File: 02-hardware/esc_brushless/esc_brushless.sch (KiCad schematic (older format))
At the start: 17 parts

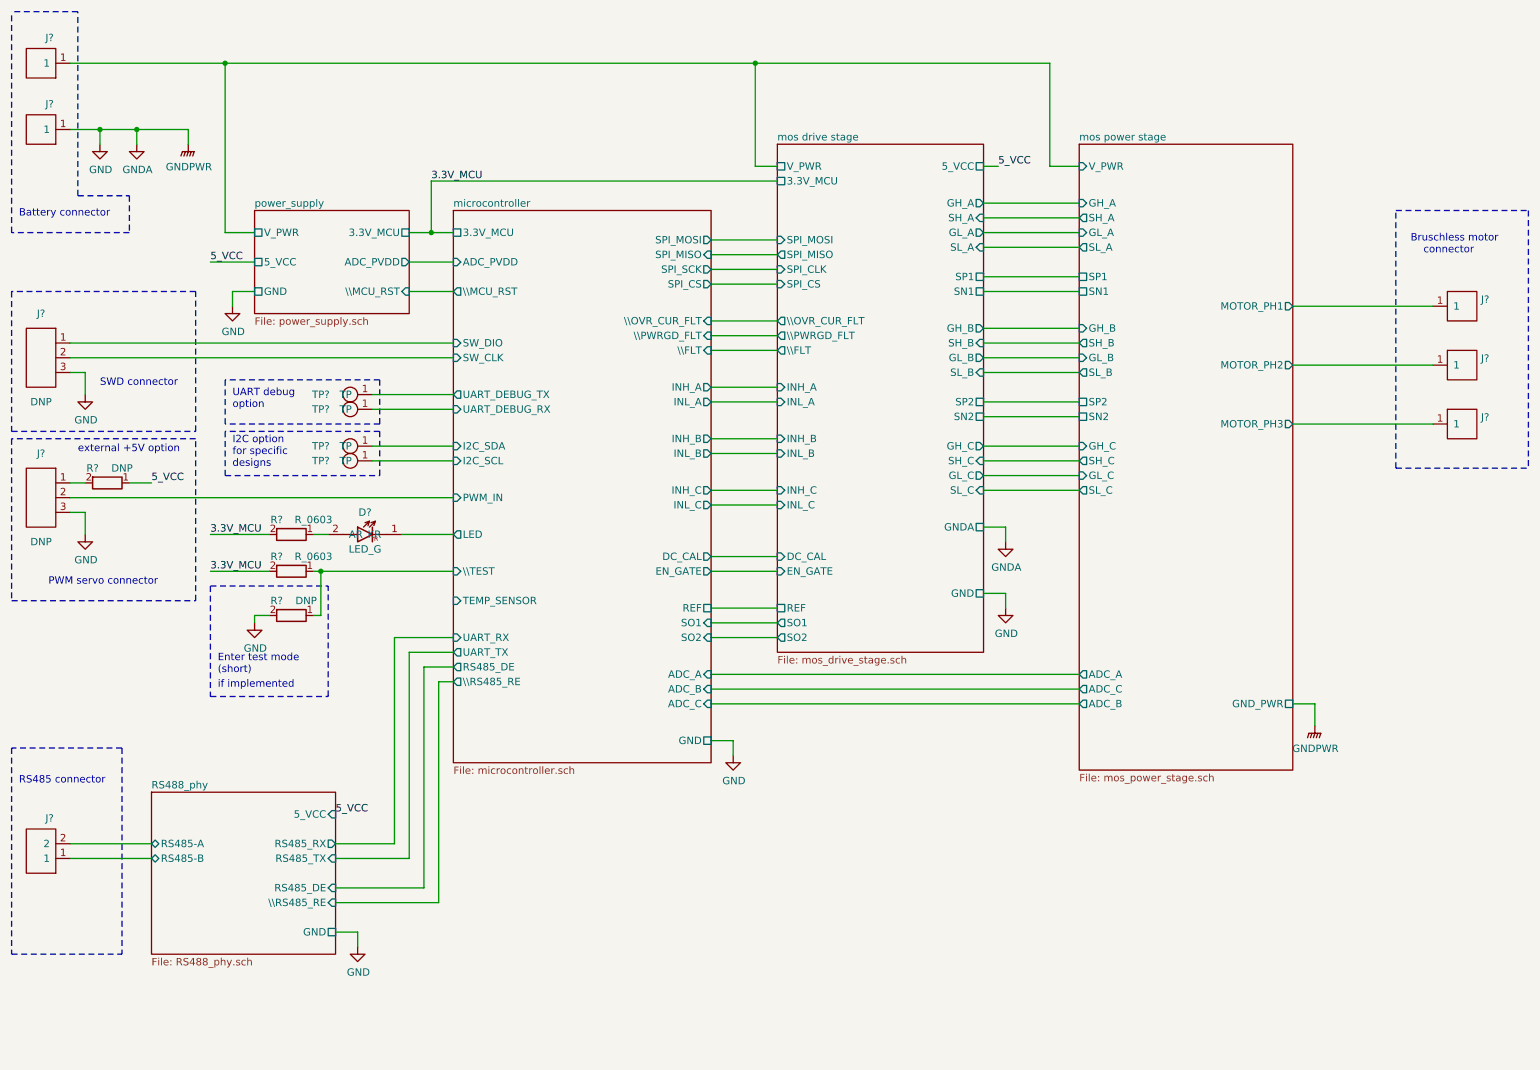
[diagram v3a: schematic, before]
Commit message: Schematics v1.0 - Fix DRC issues
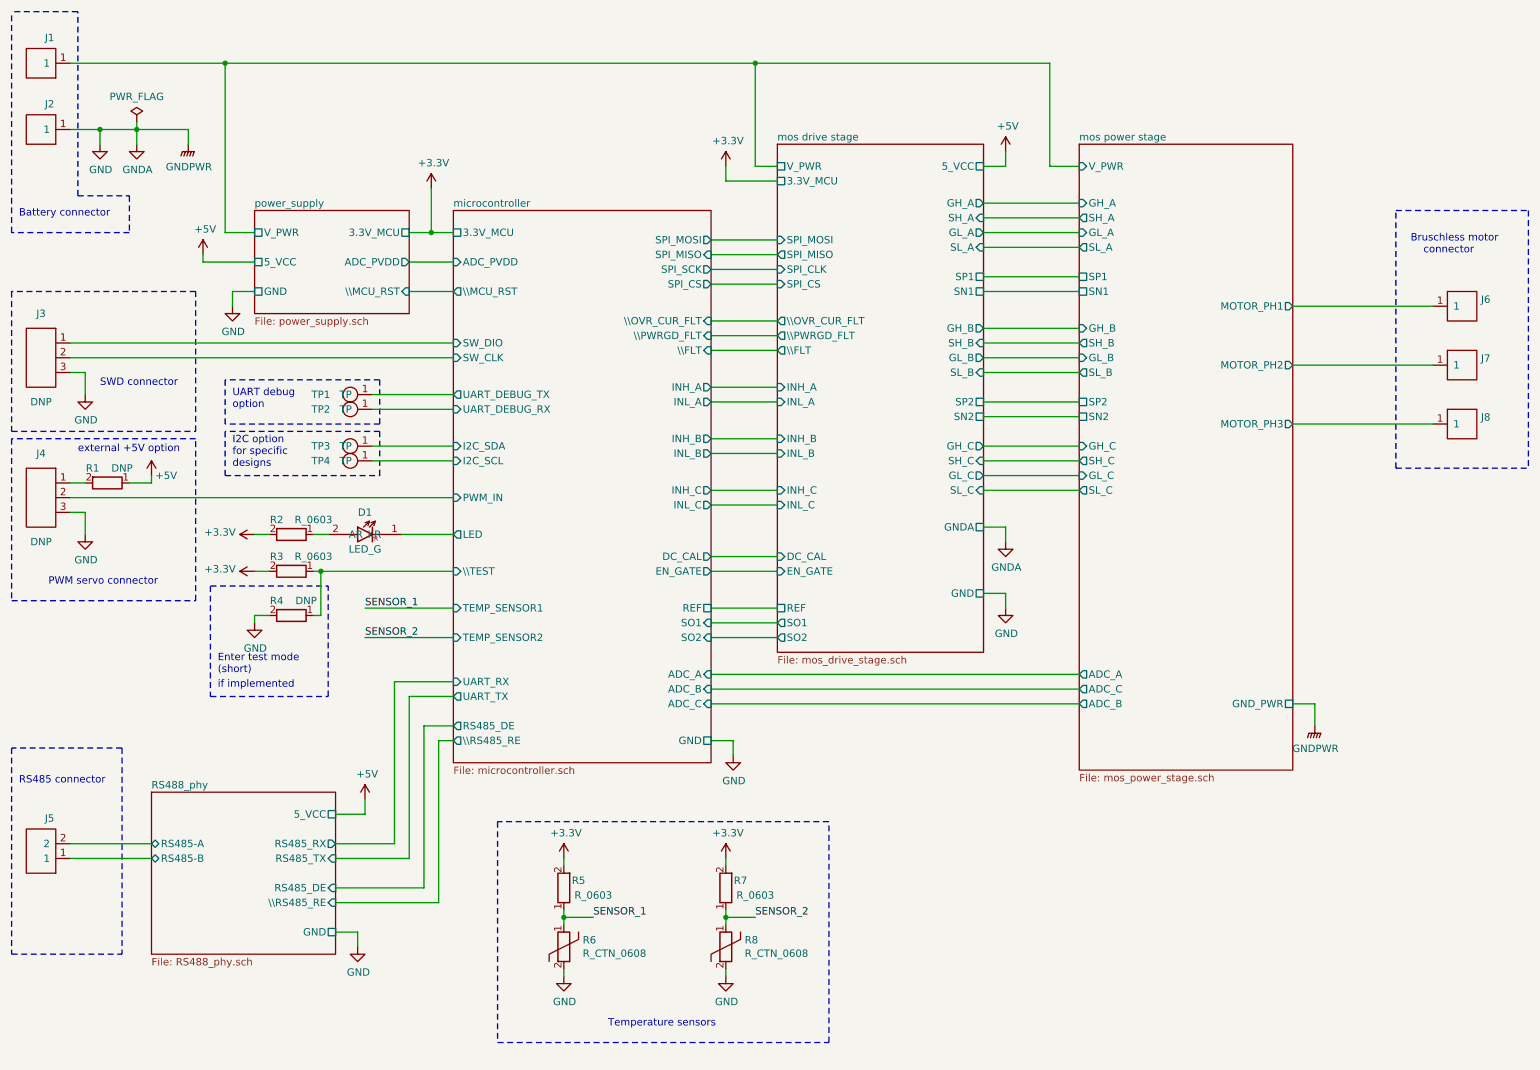
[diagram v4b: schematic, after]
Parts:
- added R5, R7: R_0603, p_Package_Resistor_SMD:R_0603_1608Metric_Pad0.98x0.95mm_HandSolder, symbol p_Passive:R_0603
- added R6, R8: R_CTN_0608, p_Package_Resistor_SMD:R_0603_1608Metric_Pad0.98x0.95mm_HandSolder, symbol p_Passive:R_CTN_0608
- gave numbers to parts that had none: 17
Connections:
- net GND: now also R6.2, R8.2
- net 3.3V_MCU renamed +3V3
- net +3V3: now also R5.2, R7.2
- net 5_VCC renamed +5V
- new net SENSOR_1: R5.1, R6.1
- new net SENSOR_2: R7.1, R8.1
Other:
- note added: "Temperature sensors"

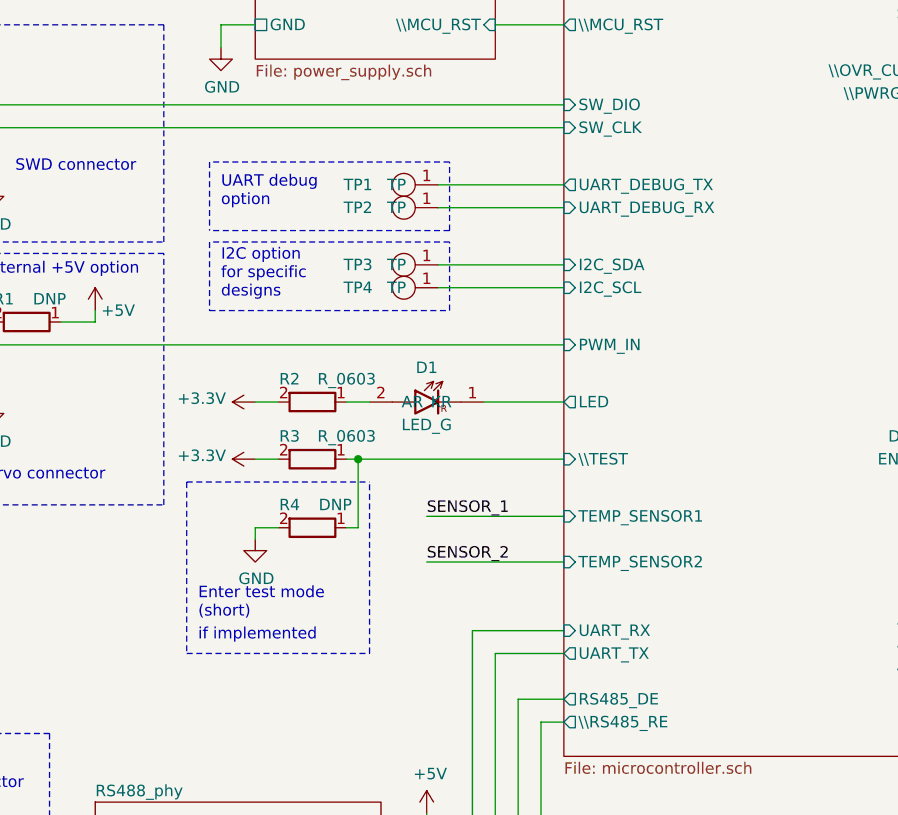
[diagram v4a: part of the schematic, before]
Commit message: Schematics v1.0 - Remove some options and test points
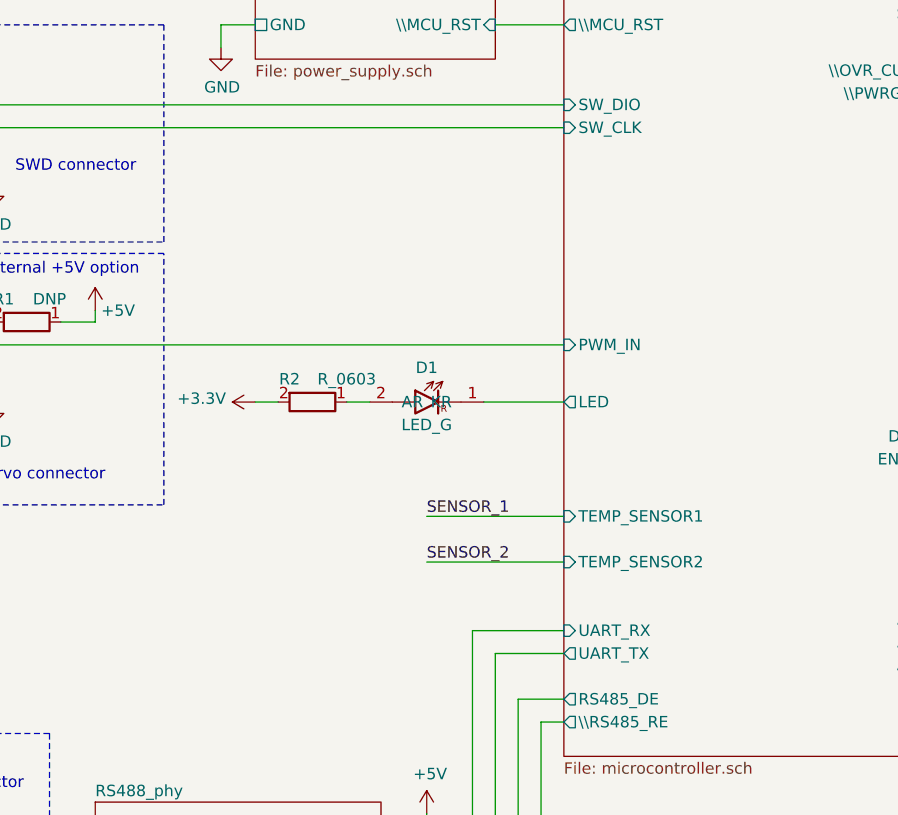
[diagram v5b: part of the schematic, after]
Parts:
- removed R3: R_0603, p_Package_Resistor_SMD:R_0603_1608Metric_Pad0.98x0.95mm_HandSolder, symbol p_Passive:R_0603
- removed R4: DNP, p_Package_Resistor_SMD:R_0603_1608Metric_Pad0.98x0.95mm_HandSolder, symbol p_Passive:R_0603
- removed TP1, TP2, TP3, TP4: test_point, p_Package_Misc:TP_SMD_1.25mm, symbol p_Misc:test_point
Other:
- note removed: "Enter test mode\n(short)"
- note removed: "I2C option \nfor specific\ndesigns"
- note removed: "UART debug\noption"
- note removed: "if implemented"
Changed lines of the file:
@@
 F22 "UART_TX" O L 3700 5250 50
 F23 "UART_RX" I L 3700 5150 50
-F24 "I2C_SDA" I L 3700 3550 50
-F25 "I2C_SCL" I L 3700 3650 50
-F26 "PWM_IN" I L 3700 3900 50
-F27 "SW_CLK" I L 3700 2950 50
-F28 "SW_DIO" I L 3700 2850 50
-F29 "ADC_PVDD" I L 3700 2300 50
-F30 "LED" O L 3700 4150 50
-F31 "\\TEST" I L 3700 4400 50
-F32 "REF" U R 5450 4650 50
-F33 "UART_DEBUG_TX" O L 3700 3200 50
-F34 "UART_DEBUG_RX" I L 3700 3300 50
-F35 "\\RS485_RE" O L 3700 5550 50
-F36 "RS485_DE" O L 3700 5450 50
-F37 "SPI_SCK" O R 5450 2350 50
-F38 "\\MCU_RST" O L 3700 2500 50
-F39 "GND" U R 5450 5550 50
-F40 "TEMP_SENSOR1" I L 3700 4650 50
-F41 "TEMP_SENSOR2" I L 3700 4850 50
+F24 "PWM_IN" I L 3700 3900 50
+F25 "SW_CLK" I L 3700 2950 50
+F26 "SW_DIO" I L 3700 2850 50
+F27 "ADC_PVDD" I L 3700 2300 50
+F28 "LED" O L 3700 4150 50
+F29 "REF" U R 5450 4650 50
+F30 "\\RS485_RE" O L 3700 5550 50
+F31 "RS485_DE" O L 3700 5450 50
+F32 "SPI_SCK" O R 5450 2350 50
+F33 "\\MCU_RST" O L 3700 2500 50
+F34 "GND" U R 5450 5550 50
+F35 "TEMP_SENSOR1" I L 3700 4650 50
+F36 "TEMP_SENSOR2" I L 3700 4850 50
 $EndSheet
 $Sheet
@@
 	-1   0    0    -1
 $EndComp
-Wire Wire Line
-	3150 3550 3700 3550
-Wire Wire Line
-	3700 3650 3150 3650
-Wire Wire Line
-	3150 3200 3700 3200
-Wire Wire Line
-	3700 3300 3150 3300
 $Comp
 L esc_brushless-rescue:Conn_HE13_1x3_2.54-p_Misc J3
@@
 $EndComp
 $Comp
-L p_Misc:test_point TP1
-U 1 1 6085C419
-P 3050 3200
-F 0 "TP1" H 2800 3200 50  0000 C CNN
-F 1 "test_point" H 3037 3334 50  0001 C CNN
-F 2 "p_Package_Misc:TP_SMD_1.25mm" H 3050 3000 50  0001 C CNN
-F 3 "" H 3050 3200 50  0001 C CNN
-	1    3050 3200
-	1    0    0    -1
-$EndComp
-$Comp
-L p_Misc:test_point TP2
-U 1 1 6085D004
-P 3050 3300
-F 0 "TP2" H 2800 3300 50  0000 C CNN
-F 1 "test_point" H 3037 3434 50  0001 C CNN
-F 2 "p_Package_Misc:TP_SMD_1.25mm" H 3050 3100 50  0001 C CNN
-F 3 "" H 3050 3300 50  0001 C CNN
-	1    3050 3300
-	1    0    0    -1
-$EndComp
-$Comp
-L p_Misc:test_point TP3
-U 1 1 6085D0A4
-P 3050 3550
-F 0 "TP3" H 2800 3550 50  0000 C CNN
-F 1 "test_point" H 3037 3684 50  0001 C CNN
-F 2 "p_Package_Misc:TP_SMD_1.25mm" H 3050 3350 50  0001 C CNN
-F 3 "" H 3050 3550 50  0001 C CNN
-	1    3050 3550
-	1    0    0    -1
-$EndComp
-$Comp
-L p_Misc:test_point TP4
-U 1 1 6085D196
-P 3050 3650
-F 0 "TP4" H 2800 3650 50  0000 C CNN
-F 1 "test_point" H 3037 3784 50  0001 C CNN
-F 2 "p_Package_Misc:TP_SMD_1.25mm" H 3050 3450 50  0001 C CNN
-F 3 "" H 3050 3650 50  0001 C CNN
-	1    3050 3650
-	1    0    0    -1
-$EndComp
-$Comp
 L power:GND #PWR01
 U 1 1 60867B73
@@
 Wire Wire Line
 	2450 4150 2350 4150
-$Comp
-L p_Passive:R_0603 R3
-U 1 1 60B8810F
-P 2600 4400
-F 0 "R3" V 2500 4300 50  0000 C CNN
-F 1 "R_0603" V 2500 4550 50  0000 C CNN
-F 2 "p_Package_Resistor_SMD:R_0603_1608Metric_Pad0.98x0.95mm_HandSolder" H 2600 4400 50  0001 C CNN
-F 3 "" H 2600 4400 50  0001 C CNN
-	1    2600 4400
-	0    1    1    0
-$EndComp
-Wire Wire Line
-	2450 4400 2350 4400
-$Comp
-L p_Passive:R_0603 R4
-U 1 1 60B93F2C
-P 2600 4700
-F 0 "R4" V 2500 4600 50  0000 C CNN
-F 1 "DNP" V 2500 4800 50  0000 C CNN
-F 2 "p_Package_Resistor_SMD:R_0603_1608Metric_Pad0.98x0.95mm_HandSolder" H 2600 4700 50  0001 C CNN
-F 3 "" H 2600 4700 50  0001 C CNN
-	1    2600 4700
-	0    1    1    0
-$EndComp
-Wire Wire Line
-	2750 4700 2800 4700
-$Comp
-L power:GND #PWR07
-U 1 1 60B9925A
-P 2350 4750
-F 0 "#PWR07" H 2350 4500 50  0001 C CNN
-F 1 "GND" H 2355 4577 50  0000 C CNN
-F 2 "" H 2350 4750 50  0001 C CNN
-F 3 "" H 2350 4750 50  0001 C CNN
-	1    2350 4750
-	1    0    0    -1
-$EndComp
-Wire Wire Line
-	2450 4700 2350 4700
-Wire Wire Line
-	2350 4700 2350 4750
-Wire Wire Line
-	2800 4700 2800 4400
 Wire Wire Line
 	3350 4150 3700 4150
-Wire Wire Line
-	2750 4400 2800 4400
-Connection ~ 2800 4400
-Wire Wire Line
-	2800 4400 3700 4400
-Wire Notes Line width 12
-	2850 5250 2850 4500
-Text Notes 2100 5100 0    50   ~ 0
-Enter test mode\n(short)
-Wire Notes Line width 12
-	2050 4500 2050 5250
-Text Notes 2100 5200 0    50   ~ 0
-if implemented
-Wire Notes Line width 12
-	2050 5250 2850 5250
-Wire Notes Line width 12
-	2050 4500 2850 4500
 $Comp
 L power:GND #PWR06
@@
 Wire Wire Line
 	2200 2500 2200 2600
-Wire Notes Line width 12
-	3200 3400 2150 3400
-Text Notes 2200 3300 0    50   ~ 0
-UART debug\noption
-Wire Notes Line width 12
-	3200 3450 2150 3450
-Wire Notes Line width 12
-	2150 3450 2150 3750
-Wire Notes Line width 12
-	2150 3750 3200 3750
-Wire Notes Line width 12
-	3200 3750 3200 3450
-Wire Notes Line width 12
-	3200 3400 3200 3100
-Wire Notes Line width 12
-	3200 3100 2150 3100
-Wire Notes Line width 12
-	2150 3100 2150 3400
-Text Notes 2200 3700 0    50   ~ 0
-I2C option \nfor specific\ndesigns
 Wire Wire Line
 	3700 5550 3600 5550
@@
 	1550 1350 1550 1400
 $Comp
-L power:+3.3V #PWR?
+L power:+3.3V #PWR0108
 U 1 1 60E602F1
 P 3550 1800
-F 0 "#PWR?" H 3550 1650 50  0001 C CNN
+F 0 "#PWR0108" H 3550 1650 50  0001 C CNN
 F 1 "+3.3V" H 3565 1973 50  0000 C CNN
 F 2 "" H 3550 1800 50  0001 C CNN
@@
 	3550 2100 3700 2100
 $Comp
-L power:+3.3V #PWR?
+L power:+3.3V #PWR0109
 U 1 1 60E68A2D
 P 5550 1650
-F 0 "#PWR?" H 5550 1500 50  0001 C CNN
+F 0 "#PWR0109" H 5550 1500 50  0001 C CNN
 F 1 "+3.3V" H 5565 1823 50  0000 C CNN
 F 2 "" H 5550 1650 50  0001 C CNN
@@
 	5550 1750 5900 1750
 $Comp
-L power:+3.3V #PWR?
+L power:+3.3V #PWR0110
 U 1 1 60ED6E72
 P 5550 6350
-F 0 "#PWR?" H 5550 6200 50  0001 C CNN
+F 0 "#PWR0110" H 5550 6200 50  0001 C CNN
 F 1 "+3.3V" H 5565 6523 50  0000 C CNN
 F 2 "" H 5550 6350 50  0001 C CNN
@@
 $EndComp
 $Comp
-L power:+3.3V #PWR?
+L power:+3.3V #PWR0111
 U 1 1 60ED8F6D
 P 4450 6350
-F 0 "#PWR?" H 4450 6200 50  0001 C CNN
+F 0 "#PWR0111" H 4450 6200 50  0001 C CNN
 F 1 "+3.3V" H 4465 6523 50  0000 C CNN
 F 2 "" H 4450 6350 50  0001 C CNN
@@
 	4450 6350 4450 6400
 $Comp
-L power:+3.3V #PWR?
+L power:+3.3V #PWR0112
 U 1 1 60EE9747
 P 2350 4150
-F 0 "#PWR?" H 2350 4000 50  0001 C CNN
+F 0 "#PWR0112" H 2350 4000 50  0001 C CNN
 F 1 "+3.3V" V 2365 4278 50  0000 L CNN
 F 2 "" H 2350 4150 50  0001 C CNN
@@
 	0    -1   -1   0
 $EndComp
-$Comp
-L power:+3.3V #PWR?
-U 1 1 60EEF11B
-P 2350 4400
-F 0 "#PWR?" H 2350 4250 50  0001 C CNN
-F 1 "+3.3V" V 2365 4528 50  0000 L CNN
-F 2 "" H 2350 4400 50  0001 C CNN
-F 3 "" H 2350 4400 50  0001 C CNN
-	1    2350 4400
-	0    -1   -1   0
-$EndComp
